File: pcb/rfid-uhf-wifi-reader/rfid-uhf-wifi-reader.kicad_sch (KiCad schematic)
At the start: 2 parts

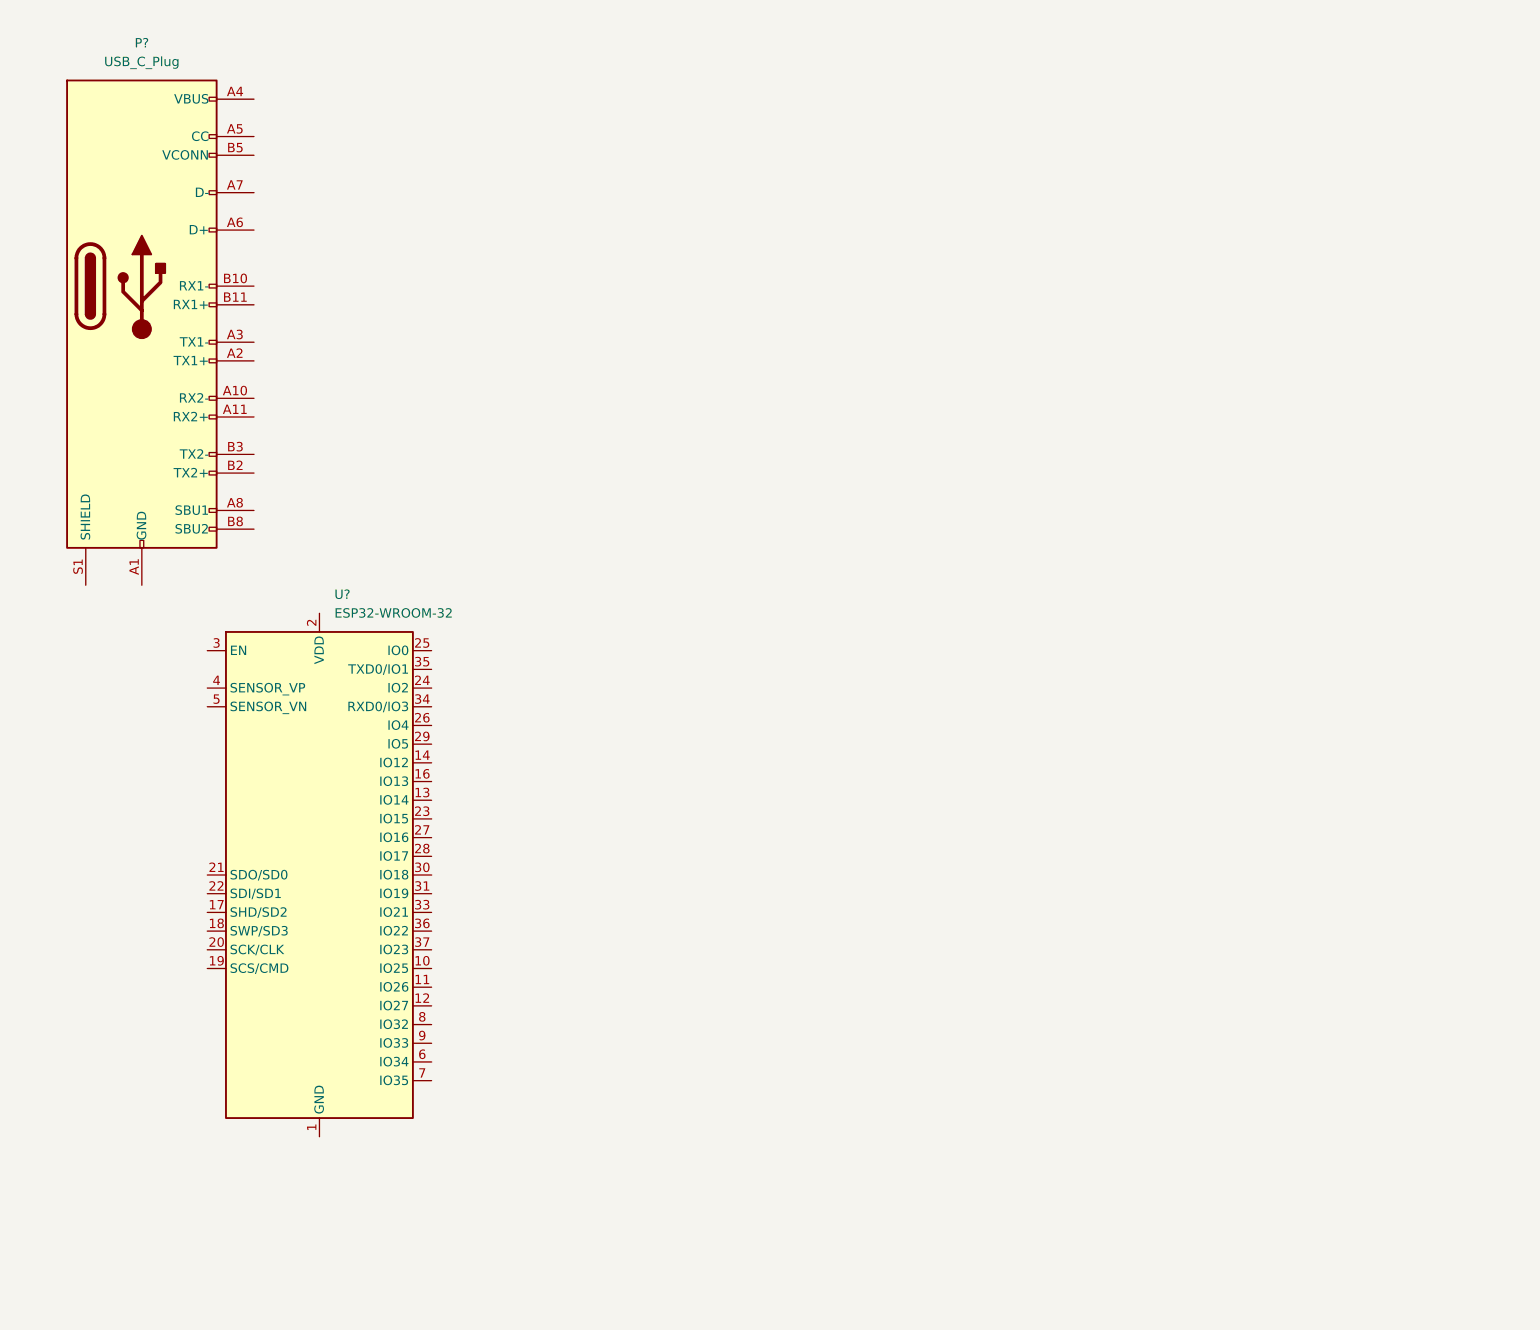
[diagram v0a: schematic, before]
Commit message: add en + prod esp32
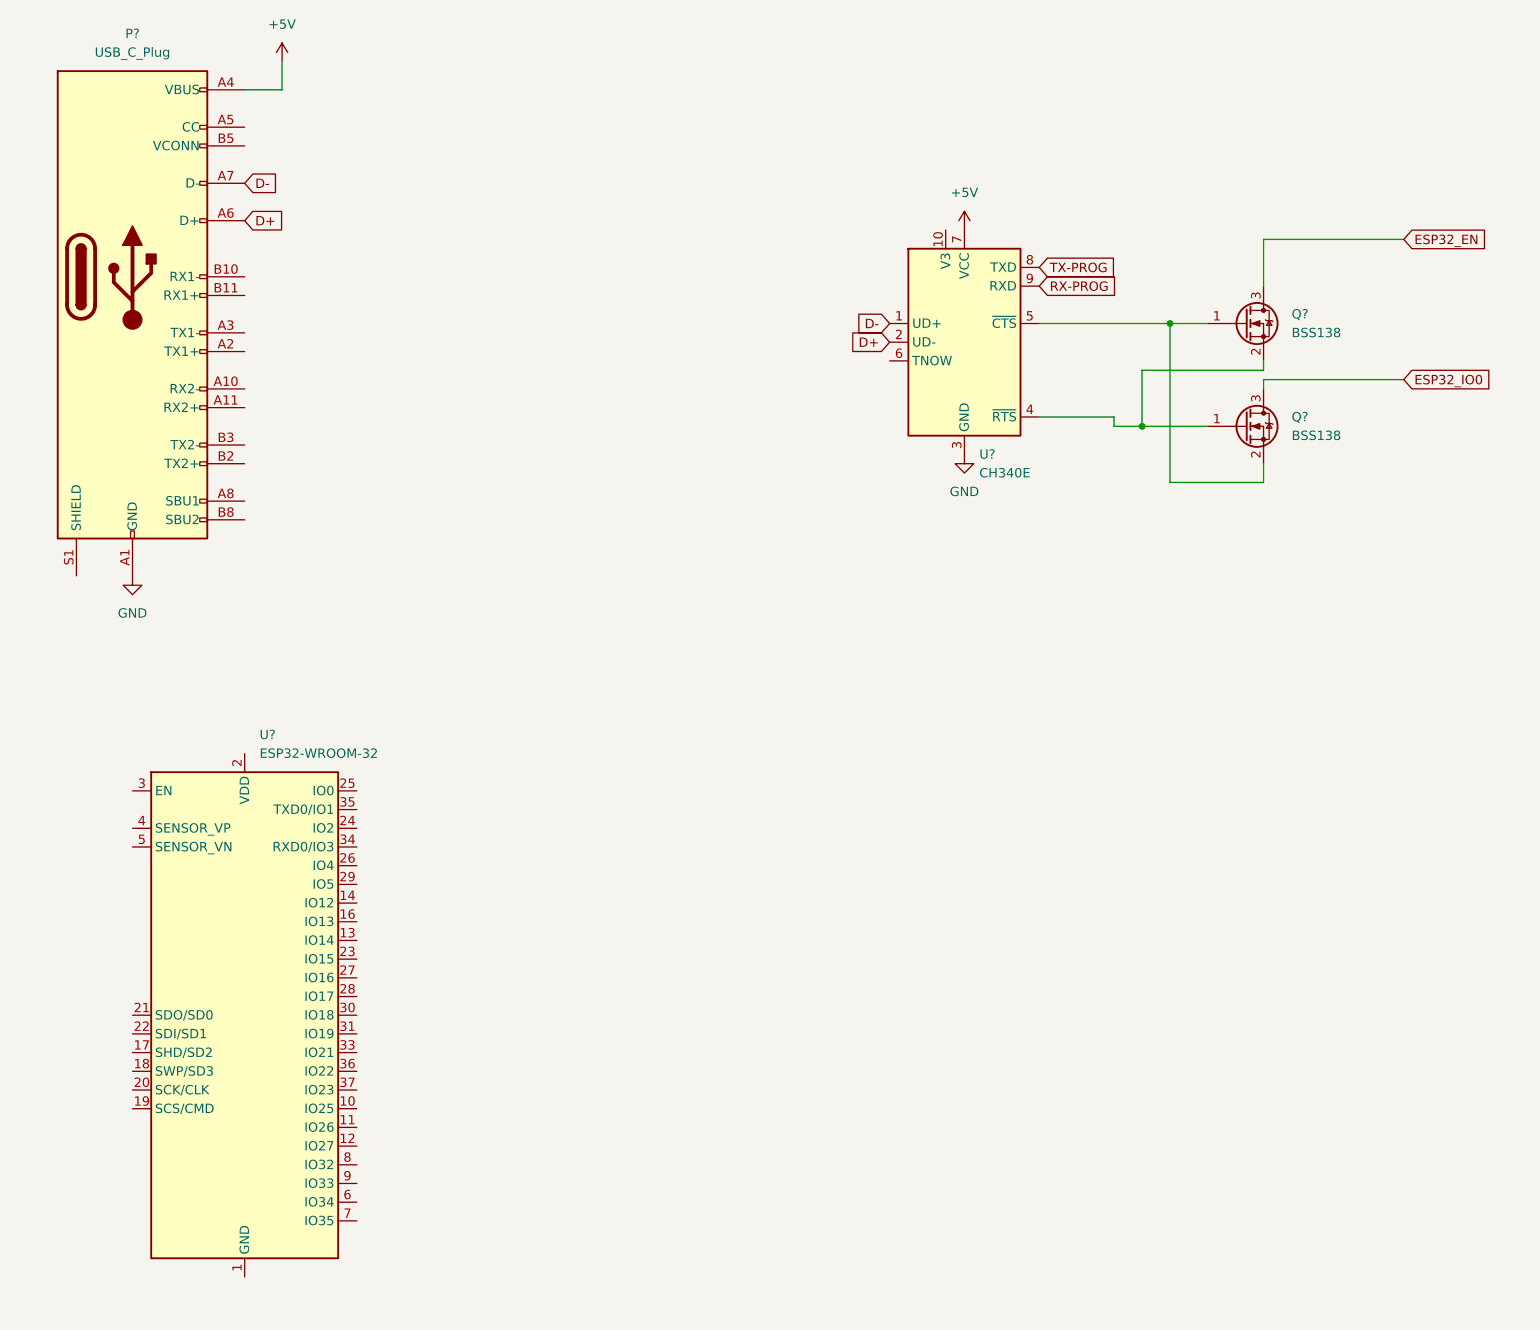
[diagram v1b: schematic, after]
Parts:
- added Q? (x2): BSS138, Package_TO_SOT_SMD:SOT-23, symbol Transistor_FET:BSS138
- added U?: CH340E, Package_SO:MSOP-10_3x3mm_P0.5mm, symbol Interface_USB:CH340E
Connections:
- net GND: now reaches P?.A1 (GND), P?.A12 (GND), P?.B1 (GND), P?.B12 (GND)
- net GND: now also U?.3 (GND)
- net +5V: now reaches P?.A4 (VBUS), P?.A9 (VBUS), P?.B4 (VBUS), P?.B9 (VBUS)
- net +5V: now also U?.7 (VCC)
- net D+: now reaches P?.A6 (D+)
- net D+: now also U?.2 (UD-)
- net D-: now reaches P?.A7 (D-)
- net D-: now also U?.1 (UD+)
- new net: Q?.1 (G), Q?.2 (S), U?.4 (~{RTS})
- new net: Q?.1 (G), Q?.2 (S), U?.5 (~{CTS})
- new net ESP32_EN: Q?.3 (D)
- new net ESP32_IO0: Q?.3 (D)
- new net RX-PROG: U?.9 (RXD)
- new net TX-PROG: U?.8 (TXD)
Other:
- moved on the sheet: P?, U?

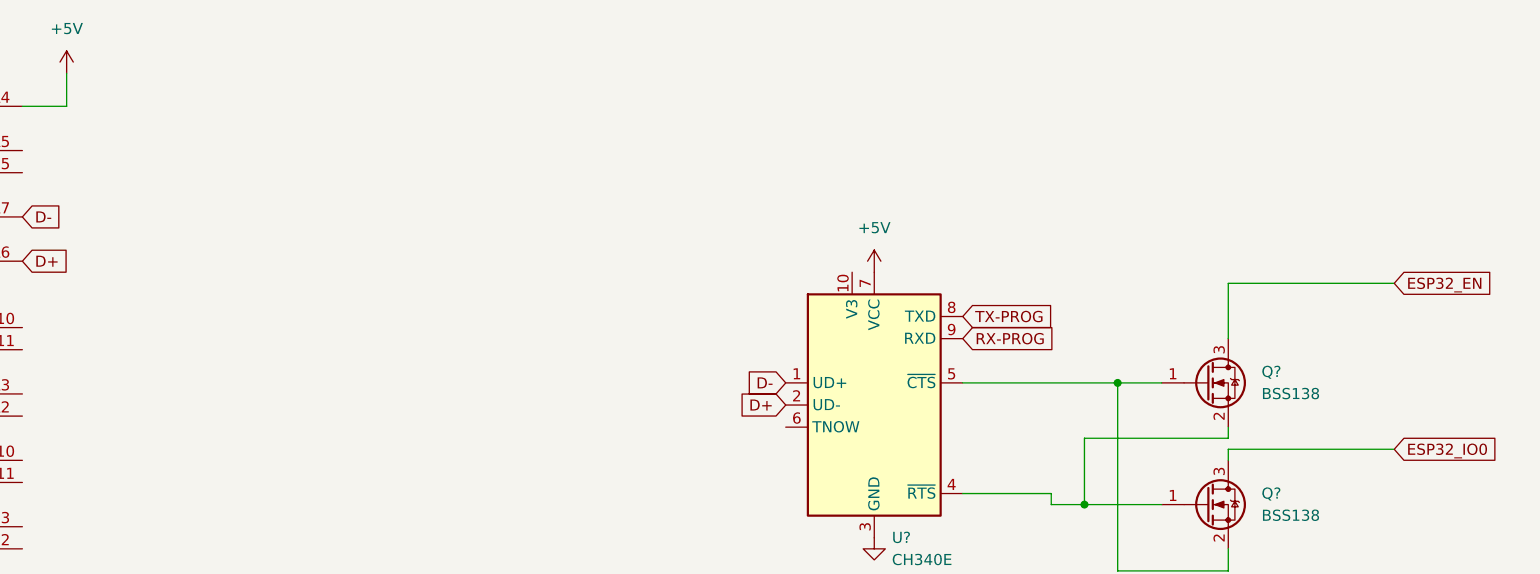
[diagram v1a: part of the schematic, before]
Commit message: add regulator
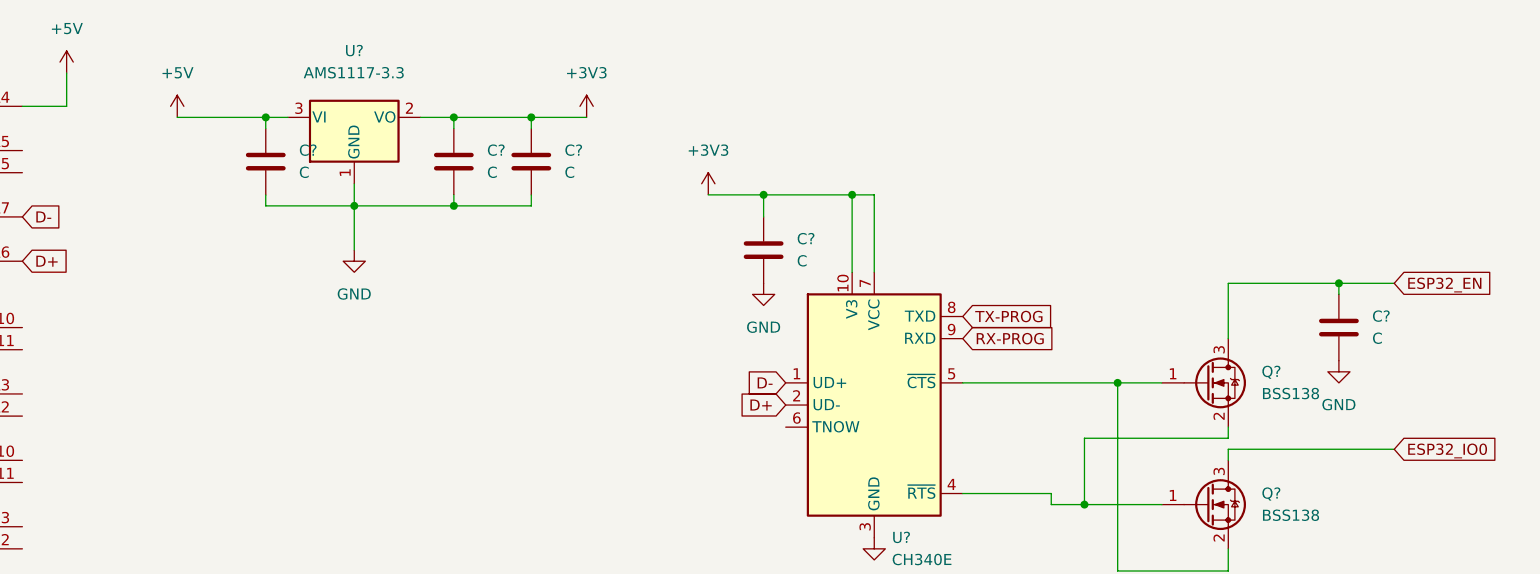
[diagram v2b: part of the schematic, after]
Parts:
- added C? (x5): C, symbol Device:C
- added U?: AMS1117-3.3, Package_TO_SOT_SMD:SOT-223-3_TabPin2, symbol Regulator_Linear:AMS1117-3.3
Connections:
- net +5V: now also C?.1, U?.3 (VI); no longer U?.7 (VCC)
- net ESP32_EN: now also C?.1
- net GND: now also C?.2, C?.2, C?.2, C?.2, C?.2, U?.1 (GND)
- net +3V3: now reaches U?.10 (V3)
- net +3V3: now also U?.7 (VCC), C?.1, C?.1, C?.1, U?.2 (VO)

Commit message: add shematic
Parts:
- added R1, R2: R_Small, Resistor_SMD:R_0603_1608Metric, symbol Device:R_Small
- added SW1, SW2: SW_Push, Button_Switch_SMD:SW_SPST_FSMSM, symbol Switch:SW_Push
- C1, C2, C3, C4, C5: renamed from C?; footprint (none) -> Capacitor_SMD:C_0603_1608Metric
- P1: renamed from P?; footprint (none) -> Connector_USB:USB_C_Plug_Molex_105444
- gave numbers to parts that had none: 5
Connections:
- net +3V3: now also R1.1, R2.1
- net ESP32_EN: now also U1.3 (EN), R1.2, SW1.2
- net ESP32_IO0: now also U1.25 (IO0), R2.2, SW2.1
- net GND: now also SW1.1, SW2.2
- net RX-PROG: now also U1.35 (TXD0/IO1)
- net TX-PROG: now also U1.34 (RXD0/IO3)
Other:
- moved on the sheet: U1
